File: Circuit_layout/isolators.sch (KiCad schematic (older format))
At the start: 28 parts, among them U17 MCP6004, U19 ACPL-C870, U20 ACPL-C870

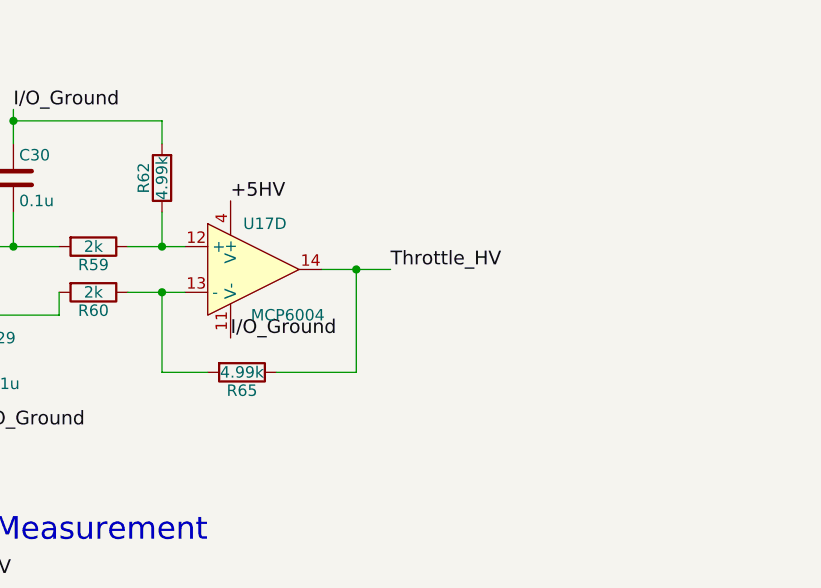
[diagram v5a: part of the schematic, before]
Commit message: eliminated warnings, need to clean things up + add footprints/datasheets
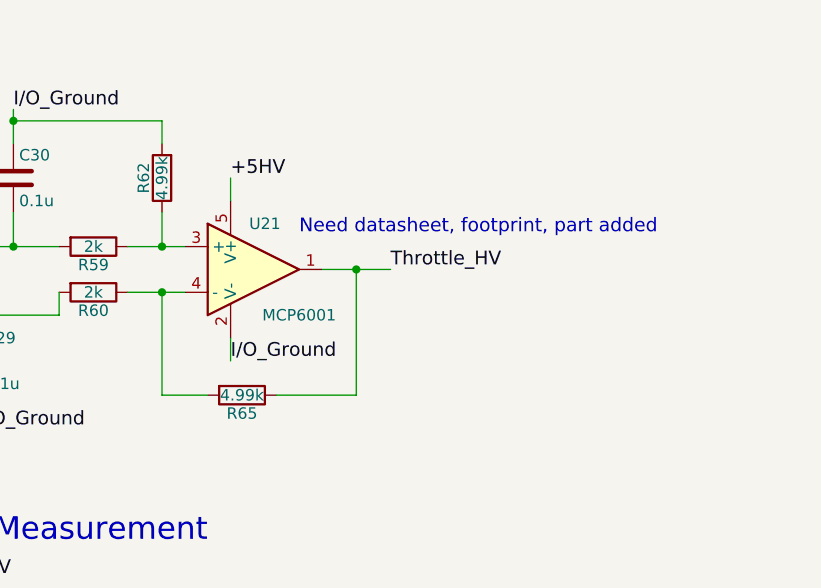
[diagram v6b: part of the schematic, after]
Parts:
- removed unit 4 of U17
- added U21: MCP6001, symbol MCP6001
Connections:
- net +5HV: now also U21.5 (V+)
- net I/O_Ground: now also U21.2 (V-)
- net Throttle_HV: now also U21.1
- net at R59.1, R62.1: now also U21.3 (+)
- net at R60.1, R65.2: now also U21.4 (-)
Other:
- note added: "Need datasheet, footprint, part added"
- moved on the sheet: R65
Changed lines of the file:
@@
 Wire Wire Line
 	4950 1600 4950 1900
-Text Label 7200 1250 0    60   ~ 0
+Text Label 7200 1150 0    60   ~ 0
 +5HV
-Text Label 7200 1850 0    60   ~ 0
+Text Label 7200 1950 0    60   ~ 0
 I/O_Ground
-Wire Wire Line
-	7100 2000 6900 2000
-Wire Wire Line
-	7400 2000 7750 2000
 Wire Wire Line
 	7600 1550 7900 1550
@@
 I/O_Ground
 Wire Wire Line
-	6900 2000 6900 1650
+	6900 1650 6900 2100
 Wire Wire Line
 	6750 1650 7000 1650
 Wire Wire Line
-	7750 2000 7750 1550
+	7750 1550 7750 2100
 Connection ~ 7750 1550
 Connection ~ 6900 1650
@@
 	3250 3950 3500 3950
 $Comp
-L +5V #PWR089
+L +5V #PWR094
 U 1 1 58B246C4
 P 4650 2700
-F 0 "#PWR089" H 4650 2550 50  0001 C CNN
+F 0 "#PWR094" H 4650 2550 50  0001 C CNN
 F 1 "+5V" H 4650 2840 50  0000 C CNN
 F 2 "" H 4650 2700 50  0000 C CNN
@@
 $EndComp
 $Comp
-L +5V #PWR090
+L +5V #PWR095
 U 1 1 58B24710
 P 4950 2900
-F 0 "#PWR090" H 4950 2750 50  0001 C CNN
+F 0 "#PWR095" H 4950 2750 50  0001 C CNN
 F 1 "+5V" H 4950 3040 50  0000 C CNN
 F 2 "" H 4950 2900 50  0000 C CNN
@@
 $EndComp
 $Comp
-L +5V #PWR091
+L +5V #PWR096
 U 1 1 58B2475C
 P 3700 3100
-F 0 "#PWR091" H 3700 2950 50  0001 C CNN
+F 0 "#PWR096" H 3700 2950 50  0001 C CNN
 F 1 "+5V" H 3700 3240 50  0000 C CNN
 F 2 "" H 3700 3100 50  0000 C CNN
@@
 $EndComp
 $Comp
-L GND #PWR092
+L GND #PWR097
 U 1 1 58B247A8
 P 3700 3700
-F 0 "#PWR092" H 3700 3450 50  0001 C CNN
+F 0 "#PWR097" H 3700 3450 50  0001 C CNN
 F 1 "GND" H 3700 3550 50  0000 C CNN
 F 2 "" H 3700 3700 50  0000 C CNN
@@
 $EndComp
 $Comp
-L GND #PWR093
+L GND #PWR098
 U 1 1 58B2480E
 P 4800 4100
-F 0 "#PWR093" H 4800 3850 50  0001 C CNN
+F 0 "#PWR098" H 4800 3850 50  0001 C CNN
 F 1 "GND" H 4800 3950 50  0000 C CNN
 F 2 "" H 4800 4100 50  0000 C CNN
@@
 	4950 1900 4650 1900
 $Comp
-L GND #PWR094
+L GND #PWR099
 U 1 1 58B25770
 P 4650 2000
-F 0 "#PWR094" H 4650 1750 50  0001 C CNN
+F 0 "#PWR099" H 4650 1750 50  0001 C CNN
 F 1 "GND" H 4650 1850 50  0000 C CNN
 F 2 "" H 4650 2000 50  0000 C CNN
@@
 $EndComp
 $Comp
-L +5V #PWR095
+L +5V #PWR0100
 U 1 1 58B257CF
 P 4950 1050
-F 0 "#PWR095" H 4950 900 50  0001 C CNN
+F 0 "#PWR0100" H 4950 900 50  0001 C CNN
 F 1 "+5V" H 4950 1190 50  0000 C CNN
 F 2 "" H 4950 1050 50  0000 C CNN
@@
 L R R65
 U 1 1 58B70BD4
-P 7250 2000
-F 0 "R65" V 7330 2000 50  0000 C CNN
-F 1 "4.99k" V 7250 2000 50  0000 C CNN
-F 2 "Resistors_SMD:R_0805_HandSoldering" V 7180 2000 50  0001 C CNN
-F 3 "" H 7250 2000 50  0000 C CNN
-F 4 "MCU0805-4.99K-MBCT-ND" V 7250 2000 60  0001 C CNN "DigiKey P/N"
-F 5 "http://www.digikey.com/product-detail/en/vishay-beyschlag/MCU0805MD4991BP100/MCU0805-4.99K-MBCT-ND/3883077" V 7250 2000 60  0001 C CNN "URL"
-F 6 "MCU0805MD4991BP100" V 7250 2000 60  0001 C CNN "Man P/N"
-	1    7250 2000
+P 7250 2100
+F 0 "R65" V 7330 2100 50  0000 C CNN
+F 1 "4.99k" V 7250 2100 50  0000 C CNN
+F 2 "Resistors_SMD:R_0805_HandSoldering" V 7180 2100 50  0001 C CNN
+F 3 "" H 7250 2100 50  0000 C CNN
+F 4 "MCU0805-4.99K-MBCT-ND" V 7250 2100 60  0001 C CNN "DigiKey P/N"
+F 5 "http://www.digikey.com/product-detail/en/vishay-beyschlag/MCU0805MD4991BP100/MCU0805-4.99K-MBCT-ND/3883077" V 7250 2100 60  0001 C CNN "URL"
+F 6 "MCU0805MD4991BP100" V 7250 2100 60  0001 C CNN "Man P/N"
+	1    7250 2100
 	0    1    1    0
 $EndComp
@@
 $Comp
 L MCP6004 U17
-U 4 1 58B3670F
-P 7300 1550
-F 0 "U17" H 7350 1750 50  0000 C CNN
-F 1 "MCP6004" H 7450 1350 50  0000 C CNN
-F 2 "Housings_SOIC:SOIC-14_3.9x8.7mm_Pitch1.27mm" H 7250 1650 50  0001 C CNN
-F 3 "http://ww1.microchip.com/downloads/en/DeviceDoc/21733j.pdf" H 7350 1750 50  0001 C CNN
-F 4 "MCP6004T-I/SLCT-ND" H 7300 1550 60  0001 C CNN "Digikey P/N"
-F 5 "http://www.digikey.com/product-detail/en/microchip-technology/MCP6004T-I-SL/MCP6004T-I-SLCT-ND/5013527" H 7300 1550 60  0001 C CNN "URL"
-F 6 "MCP6004T-I/SL" H 7300 1550 60  0001 C CNN "Man P/N"
-	4    7300 1550
-	1    0    0    -1
-$EndComp
-$Comp
-L MCP6004 U17
 U 3 1 58B367EC
 P 3600 3400
@@
 Text Label 1250 1300 0    60   ~ 0
 I/O_Ground
+Wire Wire Line
+	6900 2100 7100 2100
+Wire Wire Line
+	7750 2100 7400 2100
+Wire Wire Line
+	7200 1950 7200 1850
+Wire Wire Line
+	7200 1150 7200 1250
+$Comp
+L MCP6001 U21
+U 1 1 58B7DBA9
+P 7300 1550
+F 0 "U21" H 7350 1750 50  0000 C CNN
+F 1 "MCP6001" H 7500 1350 50  0000 C CNN
+F 2 "" H 7250 1650 50  0000 C CNN
+F 3 "" H 7350 1750 50  0000 C CNN
+	1    7300 1550
+	1    0    0    -1
+$EndComp
+Text Notes 7500 1400 0    60   ~ 0
+Need datasheet, footprint, part added
 $EndSCHEMATC
